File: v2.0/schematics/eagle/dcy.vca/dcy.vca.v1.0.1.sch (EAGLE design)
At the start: 78 parts, among them IC1 TL072P, IC2 4001N, IC3 LM324N, IC4 TL074P, IC5 4001N, IC7 TL074P, Q1 2N3704, Q2 2N3704, Q3 2N3704, Q4 2N3704, Q5 2N3906

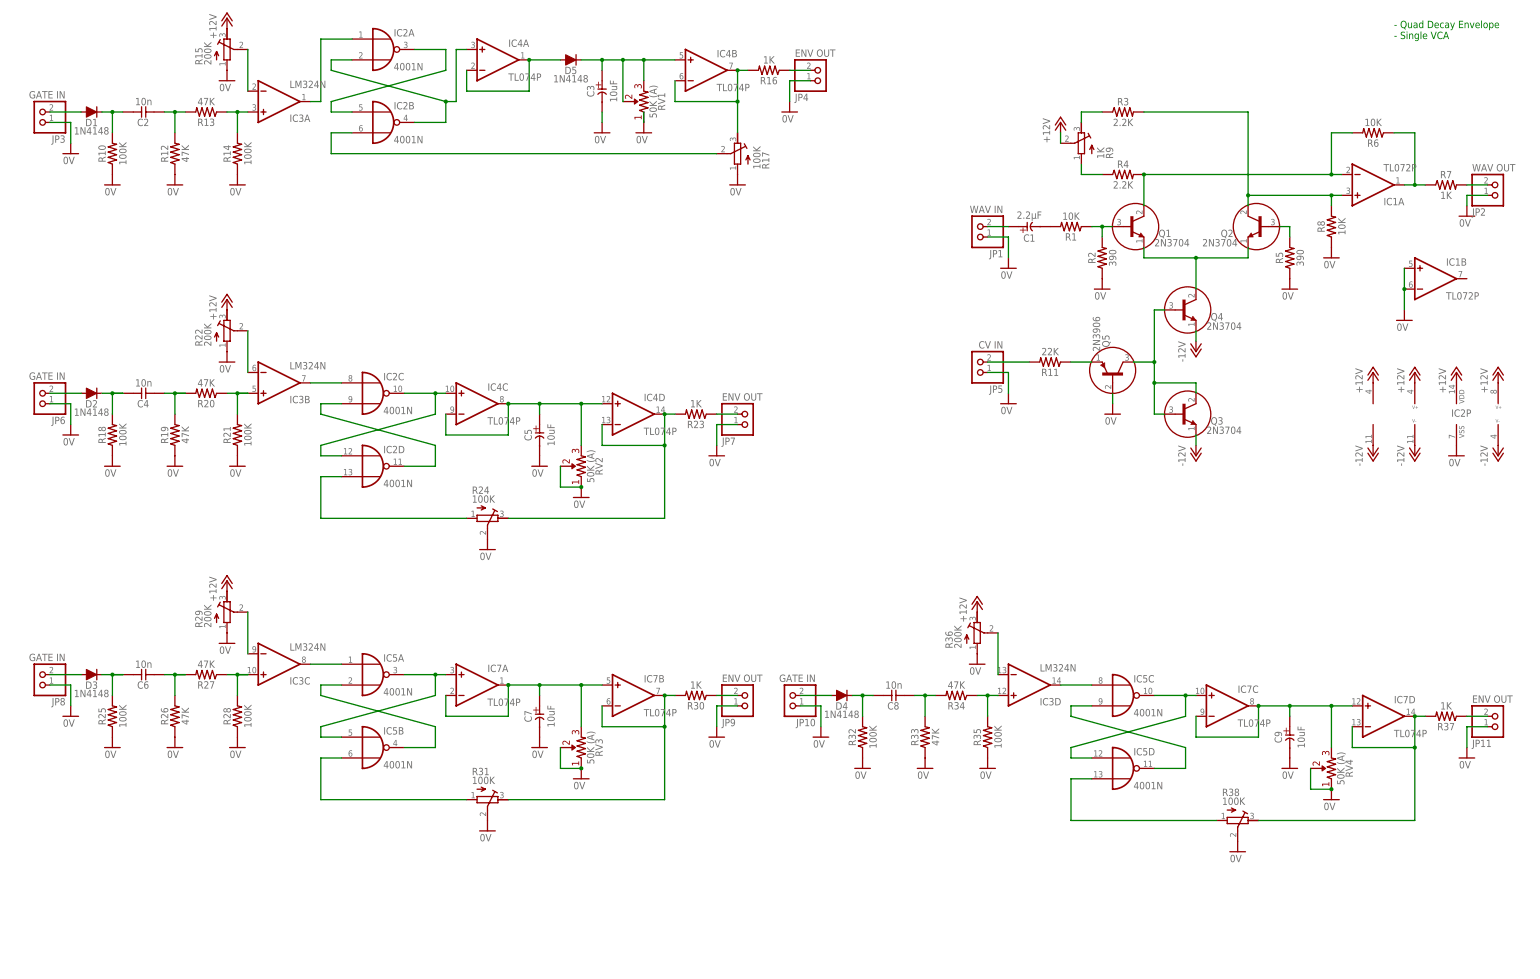
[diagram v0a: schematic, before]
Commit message: Created v1.0.1 of quad decay with tested values
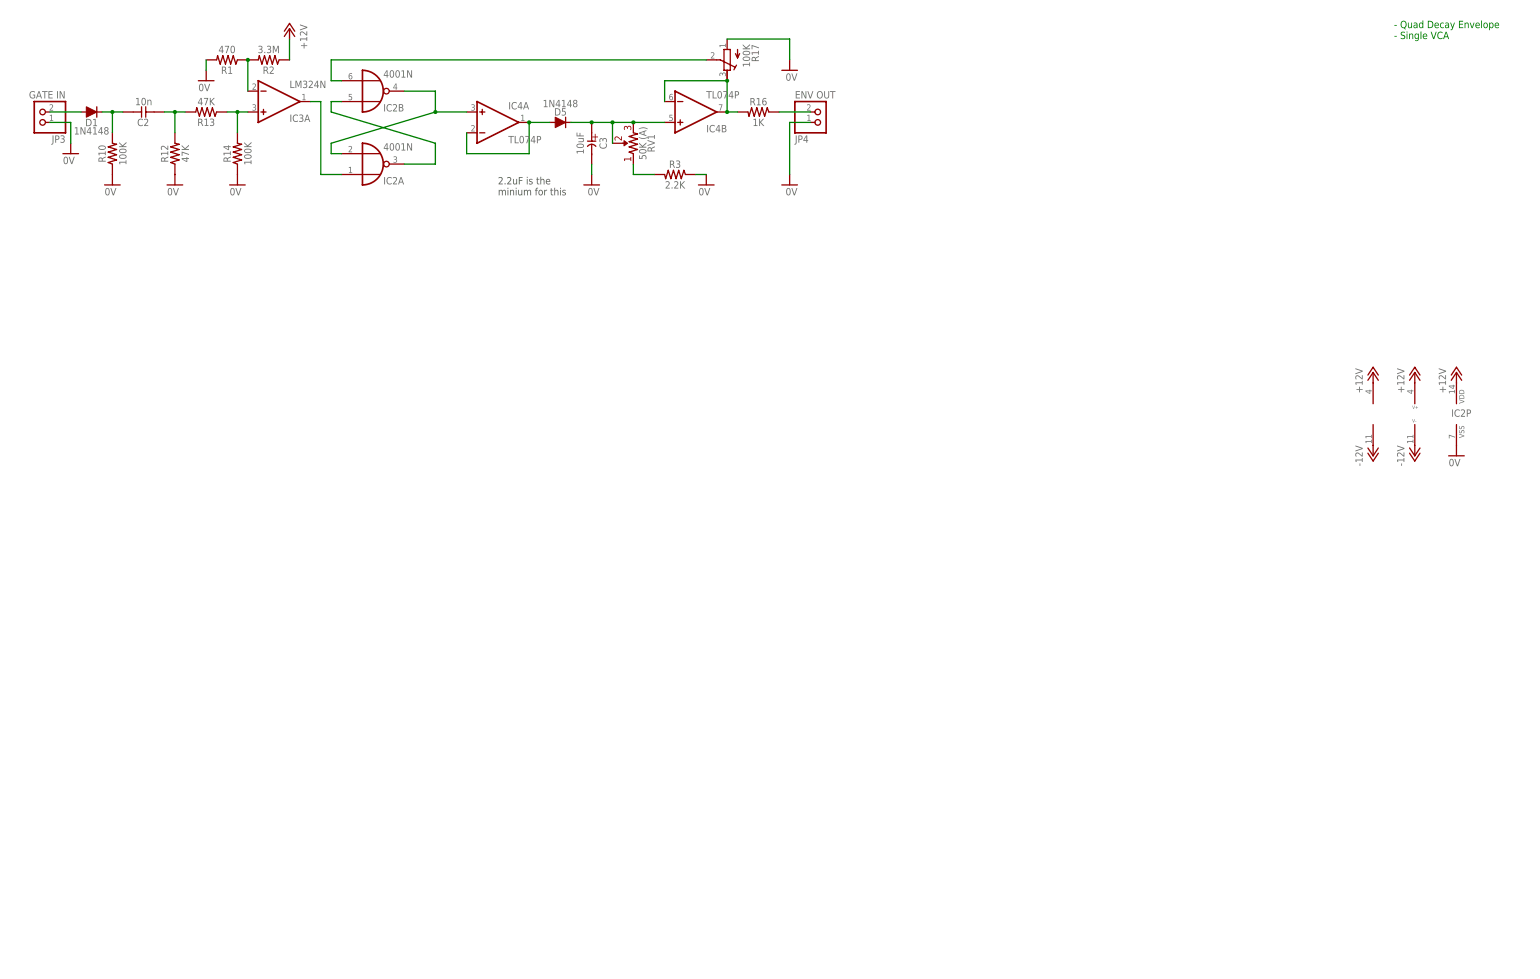
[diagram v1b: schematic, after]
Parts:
- removed C1: 2.2μF, _common:CE-USE2-5
- removed C4, C6, C8: 10n, _common:CC-US025-024X044
- removed C5, C7, C9: 10uF, _common:CE-USE2-5
- removed D2, D3, D4: 1N4148, _common:1N4148
- removed IC1: TL072P, _common:TL072P
- removed IC5: 4001N, 40xx:4001N
- removed IC7: TL074P, _common:TL074P
- removed JP1: WAV IN, pinhead:PINHD-1X2
- removed JP10, JP6, JP8: GATE IN, pinhead:PINHD-1X2
- removed JP11, JP7, JP9: ENV OUT, pinhead:PINHD-1X2
- removed JP2: WAV OUT, pinhead:PINHD-1X2
- removed JP5: CV IN, pinhead:PINHD-1X2
- removed Q1, Q2, Q3, Q4: 2N3704, _common:2N3704
- removed Q5: 2N3906, _common:2N3906
- removed R11: 22K, _common:R0309/10
- removed R15, R22, R29, R36: 200K, rcl:R-TRIMM3339P
- removed R18, R21, R25, R28, R32, R35: 100K, _common:R0309/10
- removed R19, R20, R26, R27, R33, R34: 47K, _common:R0309/10
- removed R23, R30, R37, R7: 1K, _common:R0309/10
- removed R24, R31, R38: 100K, rcl:R-TRIMM3339P
- removed R4: 2.2K, _common:R0309/10
- removed R5: 390, _common:R0309/10
- removed R6, R8: 10K, _common:R0309/10
- removed R9: 1K, rcl:R-TRIMM3339P
- removed RV2, RV3, RV4: 50K (A), _common:R-VAR
- R1: value 10K -> 470
- R2: value 390 -> 3.3M
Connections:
- removed net N$10: Q2.B, R5.2
- removed net N$11: Q1.E, Q2.E, Q4.C
- removed net N$12: Q5.E, R11.1
- removed net N$13: IC1A.OUT, R6.1, R7.1
- removed net N$16: Q3.B, Q3.C, Q4.B, Q5.C
- removed net N$2: C1.-, R1.2
- removed net N$26: JP5.2, R11.2
- removed net N$27: IC2C.O, IC2D.I0, IC4C.+IN
- removed net N$28: IC2C.I1, IC2D.O
- removed net N$29: D2.A, JP6.2
- removed net N$3: JP2.2, R7.2
- removed net N$30: C4.1, D2.C, R18.2
- removed net N$31: C4.2, R19.2, R20.2
- removed net N$32: IC3B.+IN, R20.1, R21.2
- removed net N$33: IC3B.-IN, R22.S
- removed net N$34: IC2C.I0, IC3B.OUT
- removed net N$35: C5.+, IC4C.-IN, IC4C.OUT, IC4D.+IN, RV2.2
- removed net N$36: IC4D.-IN, IC4D.OUT, R23.2, R24.E
- removed net N$37: JP7.2, R23.1
- removed net N$38: IC2D.I1, R24.A
- removed net N$39: IC5A.O, IC5B.I0, IC7A.+IN
- removed net N$40: IC5A.I1, IC5B.O
- removed net N$41: D3.A, JP8.2
- removed net N$42: C6.1, D3.C, R25.2
- removed net N$43: C6.2, R26.2, R27.2
- removed net N$44: IC3C.+IN, R27.1, R28.2
- removed net N$45: IC3C.-IN, R29.S
- removed net N$46: IC3C.OUT, IC5A.I0
- removed net N$47: C7.+, IC7A.-IN, IC7A.OUT, IC7B.+IN, RV3.2
- removed net N$48: IC7B.-IN, IC7B.OUT, R30.2, R31.E
- removed net N$49: JP9.2, R30.1
- removed net N$5: Q1.B, R1.1, R2.2
- removed net N$50: IC5B.I1, R31.A
- removed net N$51: IC5C.O, IC5D.I0, IC7C.+IN
- removed net N$52: IC5C.I1, IC5D.O
- removed net N$53: D4.A, JP10.2
- removed net N$54: C8.1, D4.C, R32.2
- removed net N$55: C8.2, R33.2, R34.2
- removed net N$56: IC3D.+IN, R34.1, R35.2
- removed net N$57: IC3D.-IN, R36.S
- removed net N$58: IC3D.OUT, IC5C.I0
- removed net N$59: C9.+, IC7C.-IN, IC7C.OUT, IC7D.+IN, RV4.2
- removed net N$6: R4.1, R9.A
- removed net N$60: IC7D.-IN, IC7D.OUT, R37.2, R38.E
- removed net N$61: JP11.2, R37.1
- removed net N$62: IC5D.I1, R38.A
- removed net N$7: R3.1, R9.E
- removed net N$8: IC1A.+IN, Q2.C, R3.2, R8.2
- removed net N$9: IC1A.-IN, Q1.C, R4.2, R6.2
- net +12V: now also R2.1; no longer IC1P.V+, R15.E, R22.E, R29.E, R36.E, R9.S
- net -12V: no longer IC1P.V-, Q3.E, Q4.E
- net 0V: now also R1.2, R3.1; no longer C5.-, C7.-, C9.-, IC1B.+IN, IC1B.-IN, JP1.1, JP10.1, JP11.1, JP2.1, JP5.1, JP6.1, JP7.1, JP8.1, JP9.1, Q5.B, R15.A, R18.1, R19.1, R2.1, R21.1, R22.A, R24.S, R25.1, R26.1, R28.1, R29.A, R31.S, R32.1, R33.1, R35.1, R36.A, R38.S, R5.1, R8.1, RV1.1, RV2.1, RV2.P$1, RV3.1, RV3.P$1, RV4.1, RV4.P$1
- net N$1: now also R3.2, RV1.1; no longer C1.+, JP1.2
- net N$21: now also R1.1, R2.2; no longer R15.S
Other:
- note added: "2.2uF is the minium for this"
- moved on the sheet: C3, D5, IC2A, IC2B, IC4A, IC4B, JP4, R1, R16, R17, R2, R3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

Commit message: Created jack package for CL1384
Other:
- note added: "- Quad Decay Envelope - Main Board"
- note removed: "- Quad Decay Envelope - Single VCA"
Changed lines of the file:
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@@
 <sheet>
 <plain>
-<text x="58.42" y="137.16" size="1.778" layer="91">- Quad Decay Envelope
-- Single VCA</text>
+<text x="55.88" y="134.62" size="1.778" layer="91">- Quad Decay Envelope
+- Main Board</text>
 <frame x1="-281.94" y1="-71.12" x2="93.98" y2="152.4" columns="8" rows="5" layer="91"/>
 <text x="-160.02" y="99.06" size="1.778" layer="97">2.2uF is the

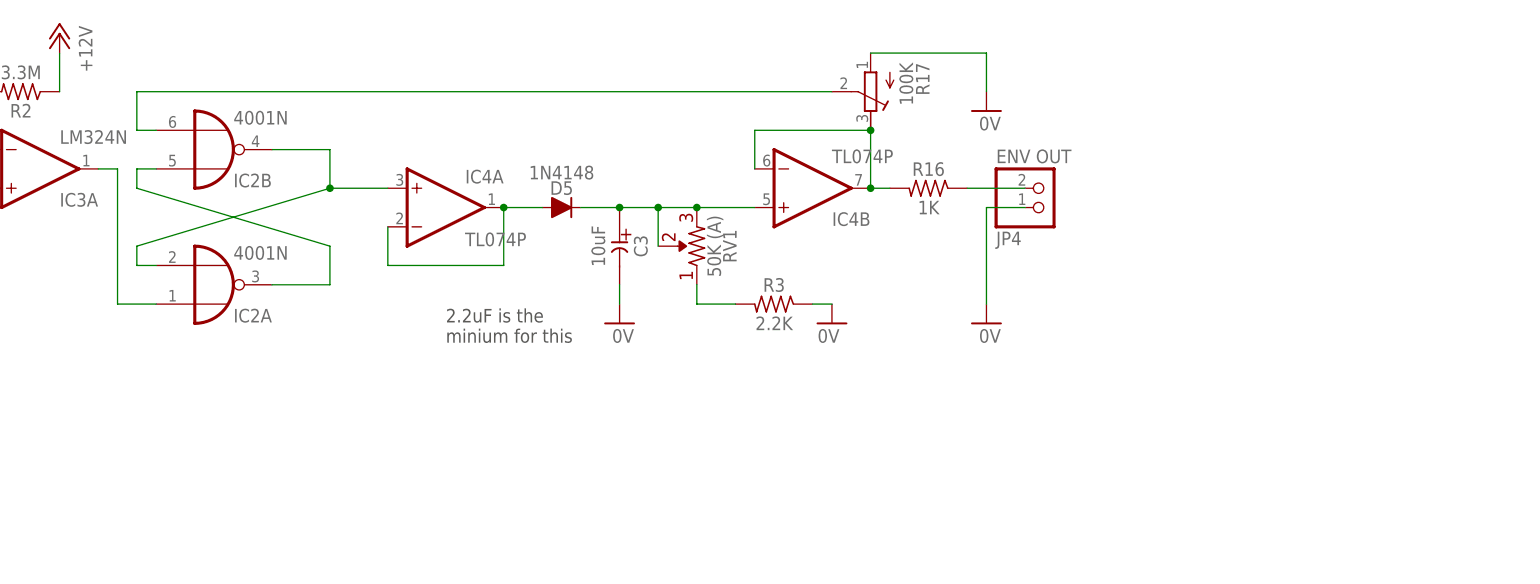
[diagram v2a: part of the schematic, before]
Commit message: Added EOC on quad decay with tested values Added Zenner diode to _common.lbr
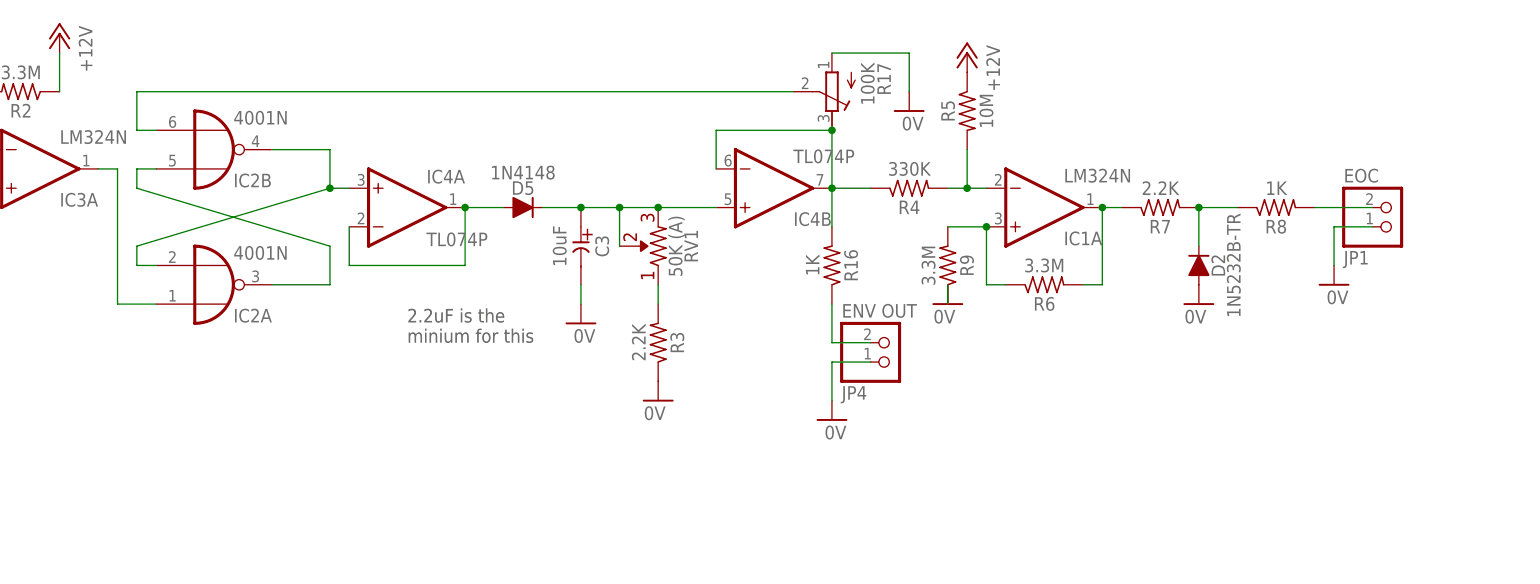
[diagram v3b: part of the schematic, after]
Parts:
- added D2: 1N5232B-TR, _common:1N5232B-TR
- added IC1: LM324N, linear:LM324N
- added JP1: EOC, pinhead:PINHD-1X2
- added R4: 330K, _common:R0309/10
- added R5: 10M, _common:R0309/10
- added R6, R9: 3.3M, _common:R0309/10
- added R7: 2.2K, _common:R0309/10
- added R8: 1K, _common:R0309/10
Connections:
- new net N$2: IC1A.-IN, R4.2, R5.2
- new net N$3: IC1A.+IN, R6.1, R9.2
- new net N$5: IC1A.OUT, R6.2, R7.1
- new net N$6: D2.C, R7.2, R8.1
- new net N$7: JP1.2, R8.2
- net +12V: now also R5.1
- net 0V: now also D2.A, JP1.1, R9.1
- net N$23: now also R4.1
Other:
- moved on the sheet: C3, D5, IC4A, IC4B, JP4, R16, R17, R3, RV1
